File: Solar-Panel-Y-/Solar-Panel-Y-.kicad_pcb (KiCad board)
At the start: 6 copper layers, 64 x 58 mm, 85 parts, among them J1 FTS-105-01-L-DV-A, J2 BM02B-SRSS-TB, Q1 BSS138DWQ-7, Q2 MBT2222ADW1T1, Q3 BSS138DWQ-7, Q4 MBT2222ADW1T1, SW1 SW_SPDT, SW2 SW_SPDT, U1 BQ25570RGRR, U2 TSL2561

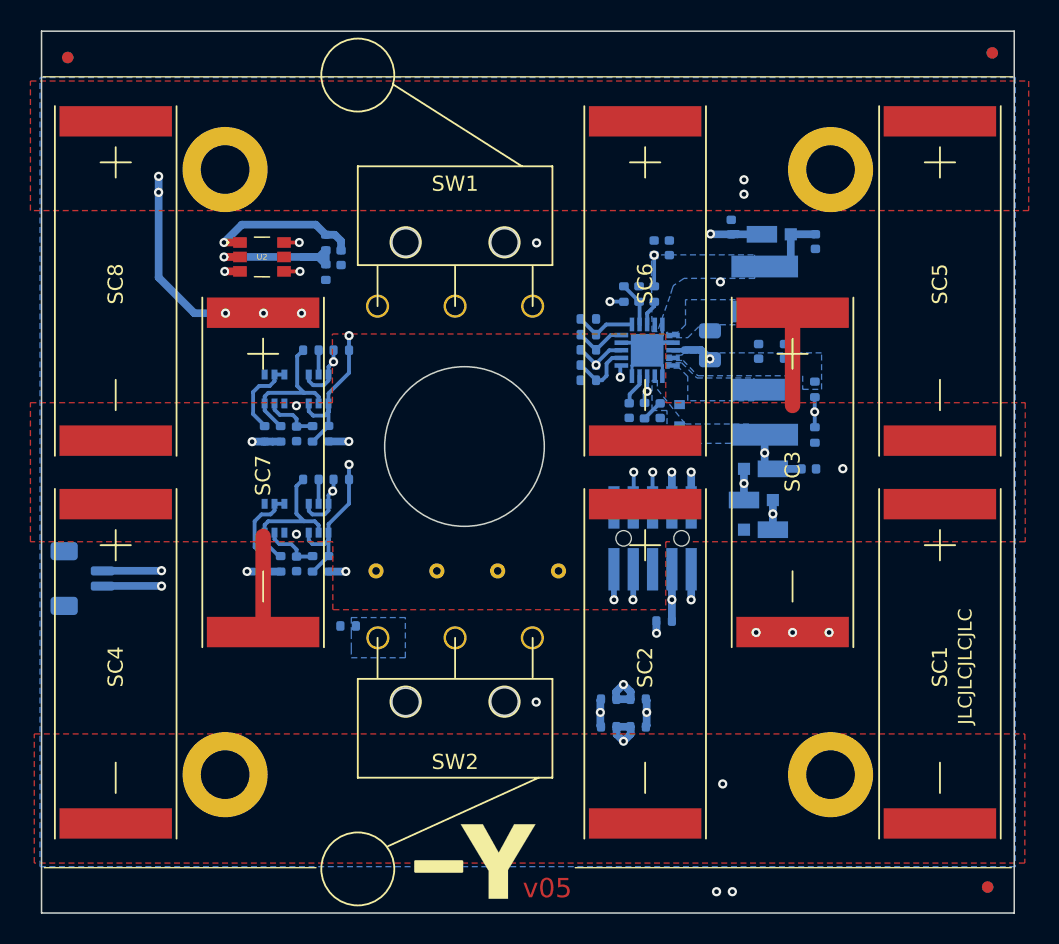
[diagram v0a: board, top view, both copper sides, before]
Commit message: Modified coil resistors on Y- board
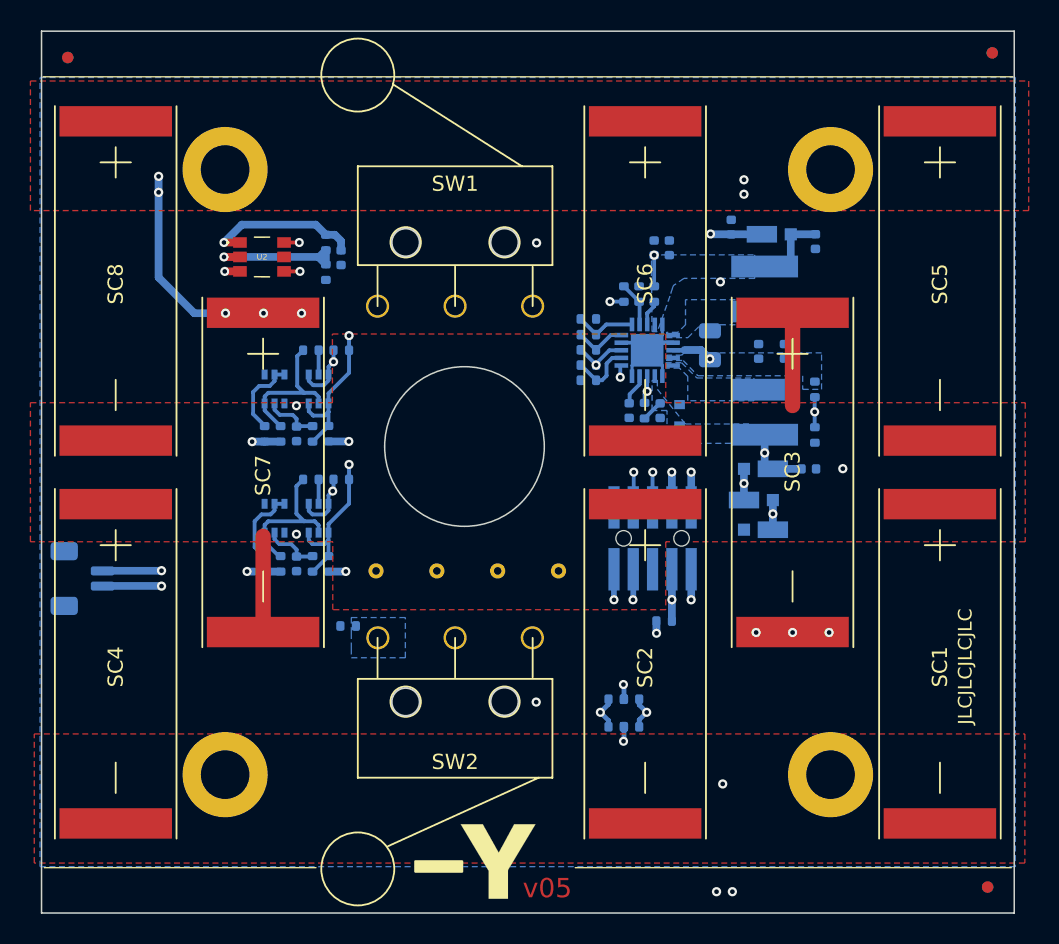
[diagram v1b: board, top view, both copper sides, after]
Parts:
- moved R13 0.49 mm to (110.6, 79.2)
- moved R18 0.49 mm to (110.6, 81.1)
- moved R12 0.44 mm to (111.6, 79.2)
- moved R17 0.44 mm to (111.6, 81.1)
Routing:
- net COIL_P: track 11.1 -> 8.83 mm
- net COIL_N: track 15.2 -> 13.0 mm
- net Net-(R1-Pad1): track 10.6 -> 9.56 mm
- net BATT_N_SW: track 49.3 -> 48.7 mm
- net SCL_LS: track 17.1 -> 16.6 mm
